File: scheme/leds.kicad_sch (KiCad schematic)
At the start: 10 parts, among them SW1 RESET, SW2 RESET

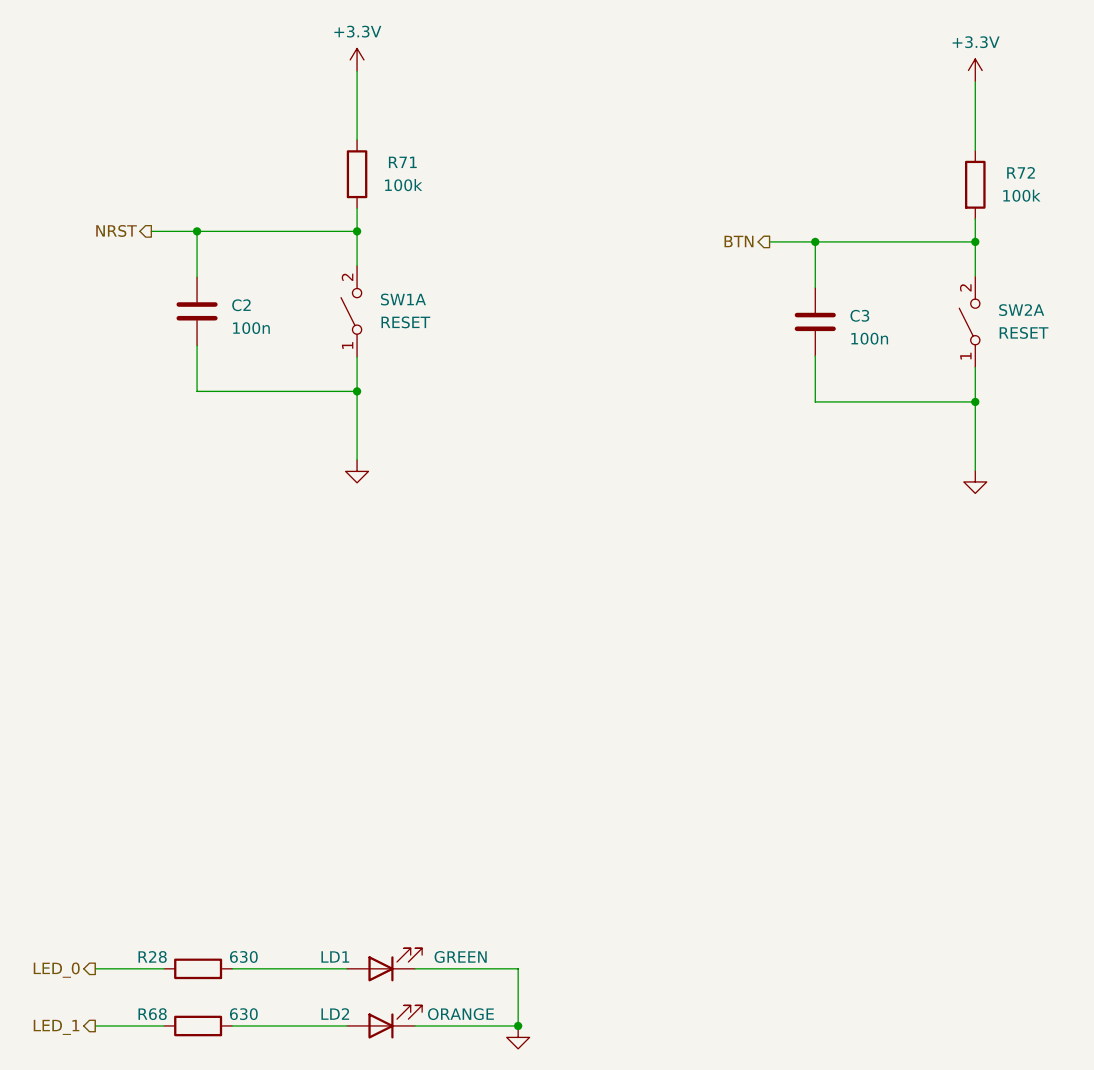
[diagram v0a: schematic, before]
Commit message: refactor(schematic): re-annotate references by sheet number
Позиционные обозначения перенумерованы по схеме «номер листа x 100»:
cpu - 1xx, st_link - 2xx, ft232rl - 3xx, w5500 - 4xx, w32 - 5xx,
tmp10x - 6xx, leds - 7xx, headers - 8xx. По обозначению на плате
сразу видно, к какому листу относится компонент.

Ссылки на компоненты в текстовых комментариях обновлены. Обозначения
из сторонних референсных схем (MB1136, MB1184, W5500-Ref, Ethernet
Shield, Adafruit) и имена выводов Arduino оставлены без изменений.

Проверено: нетлист до и после совпадает с точностью до переименования
(190 цепей, 187 компонентов), дубликатов нет, ERC - 0 ошибок.
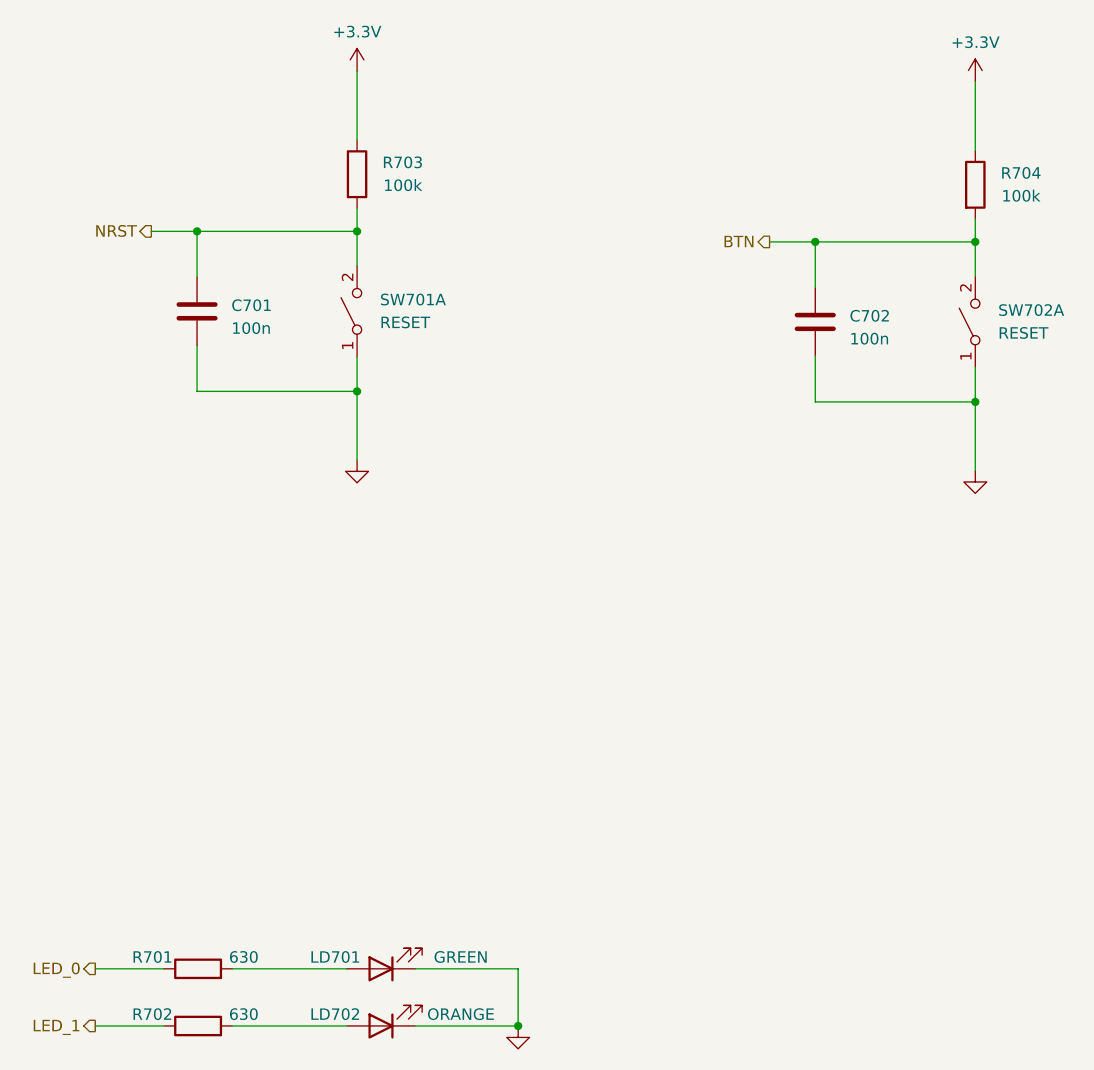
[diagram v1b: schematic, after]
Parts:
- renumbered C2 to C701, C3 to C702, LD1 to LD701, LD2 to LD702, R28 to R701, R68 to R702, R71 to R703, R72 to R704, SW1 to SW701, SW2 to SW702
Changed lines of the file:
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@@
 		(in_pos_files yes)
 		(dnp no)
-		(property "Reference" "R28"
+		(property "Reference" "R701"
 			(at 82.788 140.6069 90)
 			(show_name no)
@@
 			(project "g0_dev_board"
 				(path "/997acf0a-b54e-4c77-ad84-80f8d6e2dc27/ac24262e-e840-4a0d-aad4-70d84044d3f7"
-					(reference "R28")
+					(reference "R701")
 					(unit 1)
 				)
@@
 		(dnp no)
 		(fields_autoplaced yes)
-		(property "Reference" "#PWR095"
+		(property "Reference" "#PWR0124"
 			(at 105.53 91.6859 0)
 			(hide yes)
@@
 			(project "g0_dev_board"
 				(path "/997acf0a-b54e-4c77-ad84-80f8d6e2dc27/ac24262e-e840-4a0d-aad4-70d84044d3f7"
-					(reference "#PWR095")
+					(reference "#PWR0124")
 					(unit 1)
 				)
@@
 		(dnp no)
 		(fields_autoplaced yes)
-		(property "Reference" "C3"
+		(property "Reference" "C702"
 			(at 160.2532 69.365 0)
 			(show_name no)
@@
 			(project "g0_dev_board"
 				(path "/997acf0a-b54e-4c77-ad84-80f8d6e2dc27/ac24262e-e840-4a0d-aad4-70d84044d3f7"
-					(reference "C3")
+					(reference "C702")
 					(unit 1)
 				)
@@
 		(in_pos_files yes)
 		(dnp no)
-		(property "Reference" "R71"
+		(property "Reference" "R703"
 			(at 110.61 52.3159 0)
 			(show_name no)
@@
 			(project "g0_dev_board"
 				(path "/997acf0a-b54e-4c77-ad84-80f8d6e2dc27/ac24262e-e840-4a0d-aad4-70d84044d3f7"
-					(reference "R71")
+					(reference "R703")
 					(unit 1)
 				)
@@
 		(in_pos_files yes)
 		(dnp no)
-		(property "Reference" "R72"
+		(property "Reference" "R704"
 			(at 179.3032 53.49 0)
 			(show_name no)
@@
 			(project "g0_dev_board"
 				(path "/997acf0a-b54e-4c77-ad84-80f8d6e2dc27/ac24262e-e840-4a0d-aad4-70d84044d3f7"
-					(reference "R72")
+					(reference "R704")
 					(unit 1)
 				)
@@
 		(dnp no)
 		(fields_autoplaced yes)
-		(property "Reference" "#PWR097"
+		(property "Reference" "#PWR0127"
 			(at 174.2232 92.86 0)
 			(hide yes)
@@
 			(project "g0_dev_board"
 				(path "/997acf0a-b54e-4c77-ad84-80f8d6e2dc27/ac24262e-e840-4a0d-aad4-70d84044d3f7"
-					(reference "#PWR097")
+					(reference "#PWR0127")
 					(unit 1)
 				)
@@
 		(dnp no)
 		(fields_autoplaced yes)
-		(property "Reference" "C2"
+		(property "Reference" "C701"
 			(at 91.56 68.1909 0)
 			(show_name no)
@@
 			(project "g0_dev_board"
 				(path "/997acf0a-b54e-4c77-ad84-80f8d6e2dc27/ac24262e-e840-4a0d-aad4-70d84044d3f7"
-					(reference "C2")
+					(reference "C701")
 					(unit 1)
 				)
@@
 		(dnp no)
 		(fields_autoplaced yes)
-		(property "Reference" "#PWR039"
+		(property "Reference" "#PWR0123"
 			(at 105.53 45.9659 0)
 			(hide yes)
@@
 			(project "g0_dev_board"
 				(path "/997acf0a-b54e-4c77-ad84-80f8d6e2dc27/ac24262e-e840-4a0d-aad4-70d84044d3f7"
-					(reference "#PWR039")
+					(reference "#PWR0123")
 					(unit 1)
 				)
@@
 		(in_pos_files yes)
 		(dnp no)
-		(property "Reference" "LD1"
+		(property "Reference" "LD701"
 			(at 103.108 140.6069 0)
 			(show_name no)
@@
 			(project "g0_dev_board"
 				(path "/997acf0a-b54e-4c77-ad84-80f8d6e2dc27/ac24262e-e840-4a0d-aad4-70d84044d3f7"
-					(reference "LD1")
+					(reference "LD701")
 					(unit 1)
 				)
@@
 		(in_pos_files yes)
 		(dnp no)
-		(property "Reference" "LD2"
+		(property "Reference" "LD702"
 			(at 103.108 146.9569 0)
 			(show_name no)
@@
 			(project "g0_dev_board"
 				(path "/997acf0a-b54e-4c77-ad84-80f8d6e2dc27/ac24262e-e840-4a0d-aad4-70d84044d3f7"
-					(reference "LD2")
+					(reference "LD702")
 					(unit 1)
 				)
@@
 		(dnp no)
 		(fields_autoplaced yes)
-		(property "Reference" "#PWR096"
+		(property "Reference" "#PWR0126"
 			(at 174.2232 47.14 0)
 			(hide yes)
@@
 			(project "g0_dev_board"
 				(path "/997acf0a-b54e-4c77-ad84-80f8d6e2dc27/ac24262e-e840-4a0d-aad4-70d84044d3f7"
-					(reference "#PWR096")
+					(reference "#PWR0126")
 					(unit 1)
 				)
@@
 		(in_pos_files yes)
 		(dnp no)
-		(property "Reference" "SW1"
+		(property "Reference" "SW701"
 			(at 108.07 67.5559 90)
 			(show_name no)
@@
 			(project "g0_dev_board"
 				(path "/997acf0a-b54e-4c77-ad84-80f8d6e2dc27/ac24262e-e840-4a0d-aad4-70d84044d3f7"
-					(reference "SW1")
+					(reference "SW701")
 					(unit 1)
 				)
@@
 		(in_pos_files yes)
 		(dnp no)
-		(property "Reference" "SW2"
+		(property "Reference" "SW702"
 			(at 176.7632 68.73 90)
 			(show_name no)
@@
 			(project "g0_dev_board"
 				(path "/997acf0a-b54e-4c77-ad84-80f8d6e2dc27/ac24262e-e840-4a0d-aad4-70d84044d3f7"
-					(reference "SW2")
+					(reference "SW702")
 					(unit 1)
 				)
@@
 		(in_pos_files yes)
 		(dnp no)
-		(property "Reference" "R68"
+		(property "Reference" "R702"
 			(at 82.788 146.9569 90)
 			(show_name no)
@@
 			(project "g0_dev_board"
 				(path "/997acf0a-b54e-4c77-ad84-80f8d6e2dc27/ac24262e-e840-4a0d-aad4-70d84044d3f7"
-					(reference "R68")
+					(reference "R702")
 					(unit 1)
 				)
@@
 		(dnp no)
 		(fields_autoplaced yes)
-		(property "Reference" "#PWR094"
+		(property "Reference" "#PWR0125"
 			(at 123.428 154.5769 0)
 			(hide yes)
@@
 			(project "g0_dev_board"
 				(path "/997acf0a-b54e-4c77-ad84-80f8d6e2dc27/ac24262e-e840-4a0d-aad4-70d84044d3f7"
-					(reference "#PWR094")
-					(unit 1)
-				)
+					(reference "#PWR0125")
+					(unit 1)
+				)

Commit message: fix(schematic): resolve all ERC warnings
ERC: 0 ошибок, 0 предупреждений (было 239 предупреждений).

- w5500, leds: все объекты перенесены на сетку 1.27 мм; удалены
  два провода нулевой длины.
- Заведена проектная библиотека g0_dev_board.kicad_sym (+ sym-lib-table)
  для намеренно изменённых символов: USB_B_Mini с пассивными
  VBUS/GND (J201, J301). Попутно исправлен номер вывода экрана
  6 -> SH: у footprint Lumberg 2486 01 площадки экрана называются SH,
  иначе экран на плате остался бы неподключённым.
- Устаревшие копии символа LED обновлены из стандартной библиотеки.
- Кнопки SW701/SW702: SW_DPST_x2 заменён на SW_Push, footprint
  SW_SPST_PTS645Sx43SMTR92 (площадки 1,1,2,2 уже попарно замкнуты).
- Флэш U501: WP и HOLD подтянуты к +3.3V через R516/R517 10k
  вместо прямого подключения к выходу LDO.

Связность проверена сравнением нетлистов: изменились только цепи
WP/HOLD флэша.
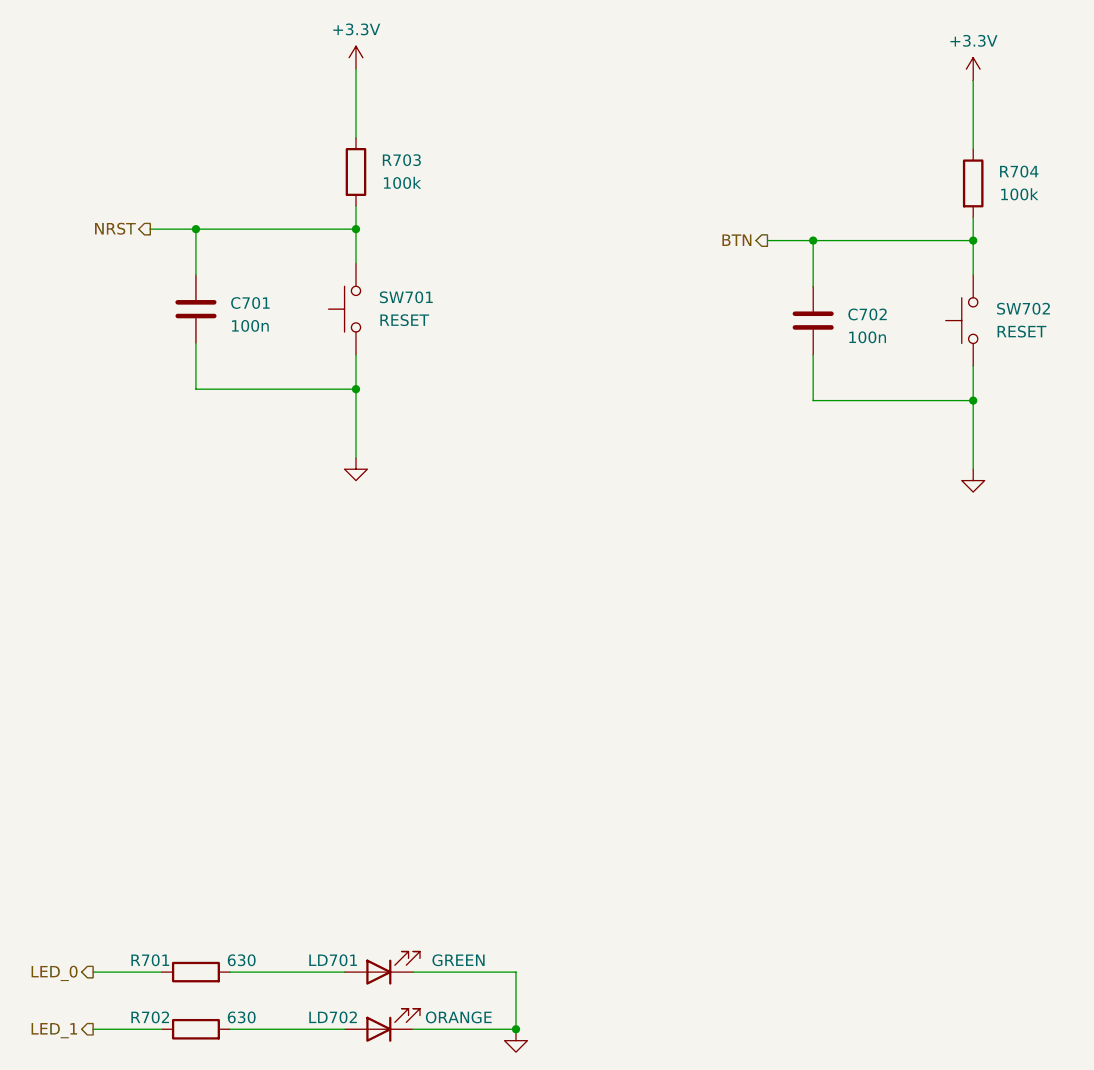
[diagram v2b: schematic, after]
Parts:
- SW701, SW702: footprint Button_Switch_SMD:SW_SPST_PTS645 -> Button_Switch_SMD:SW_SPST_PTS645Sx43SMTR92; symbol Switch:SW_DPST_x2 -> Switch:SW_Push

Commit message: fix(schematic): harden FT232 reset and reduce NRST load
- FT232RL: делитель RESET# R302/R303 4.7k/10k -> 1k/2.2k. Обратная
  утечка Шоттки D301 при питании платы от ST-Link поднимала RESET#
  к порогу; теперь порог достигается при 0.59 мА, что выше
  гарантированного IR max B120.
- ST-Link: PTC F201 MF-MSMF050 -> MF-MSMF075 (R1max 1.0 -> 0.45 Ом),
  чтобы VCC FT232 оставался >= 4.0 В в худшем случае.
- NRST: C701 и R703 на листе leds -> DNP. Остаются C103 100n у вывода
  и внутренняя подтяжка, как рекомендует ST (DS13560 рис. 27) и как на
  NUCLEO MB1136.
- SW702: значение RESET -> USER (это пользовательская кнопка на PC13).

Комментарии на схеме обновлены. ERC: 0 ошибок, 0 предупреждений.
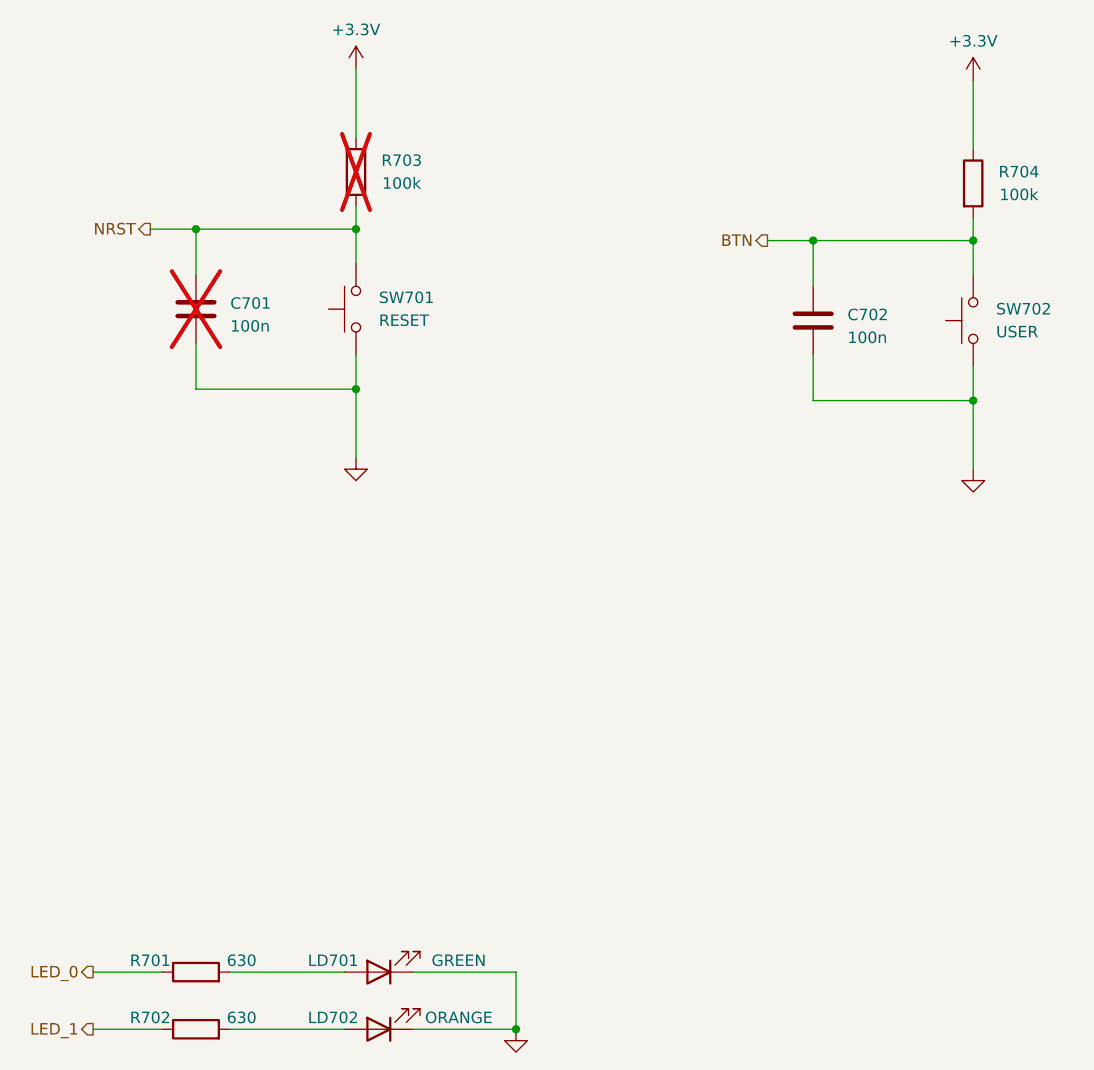
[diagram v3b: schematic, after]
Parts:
- C701, R703: now not fitted
- SW702: value RESET -> USER
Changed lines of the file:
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@@
 		(on_board yes)
 		(in_pos_files yes)
-		(dnp no)
+		(dnp yes)
 		(property "Reference" "R703"
 			(at 110.49 52.07 0)
@@
 		(on_board yes)
 		(in_pos_files yes)
-		(dnp no)
+		(dnp yes)
 		(fields_autoplaced yes)
 		(property "Reference" "C701"
@@
 			)
 		)
-		(property "Value" "RESET"
+		(property "Value" "USER"
 			(at 176.53 71.12 90)
 			(show_name no)
